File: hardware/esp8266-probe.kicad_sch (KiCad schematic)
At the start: 31 parts, among them J1 USB_C_Receptacle_USB2.0, J2 Debug, J3 Target, SW1 Reset, SW2 Flash, U1 LD1117DT33, U2 ESP-12E

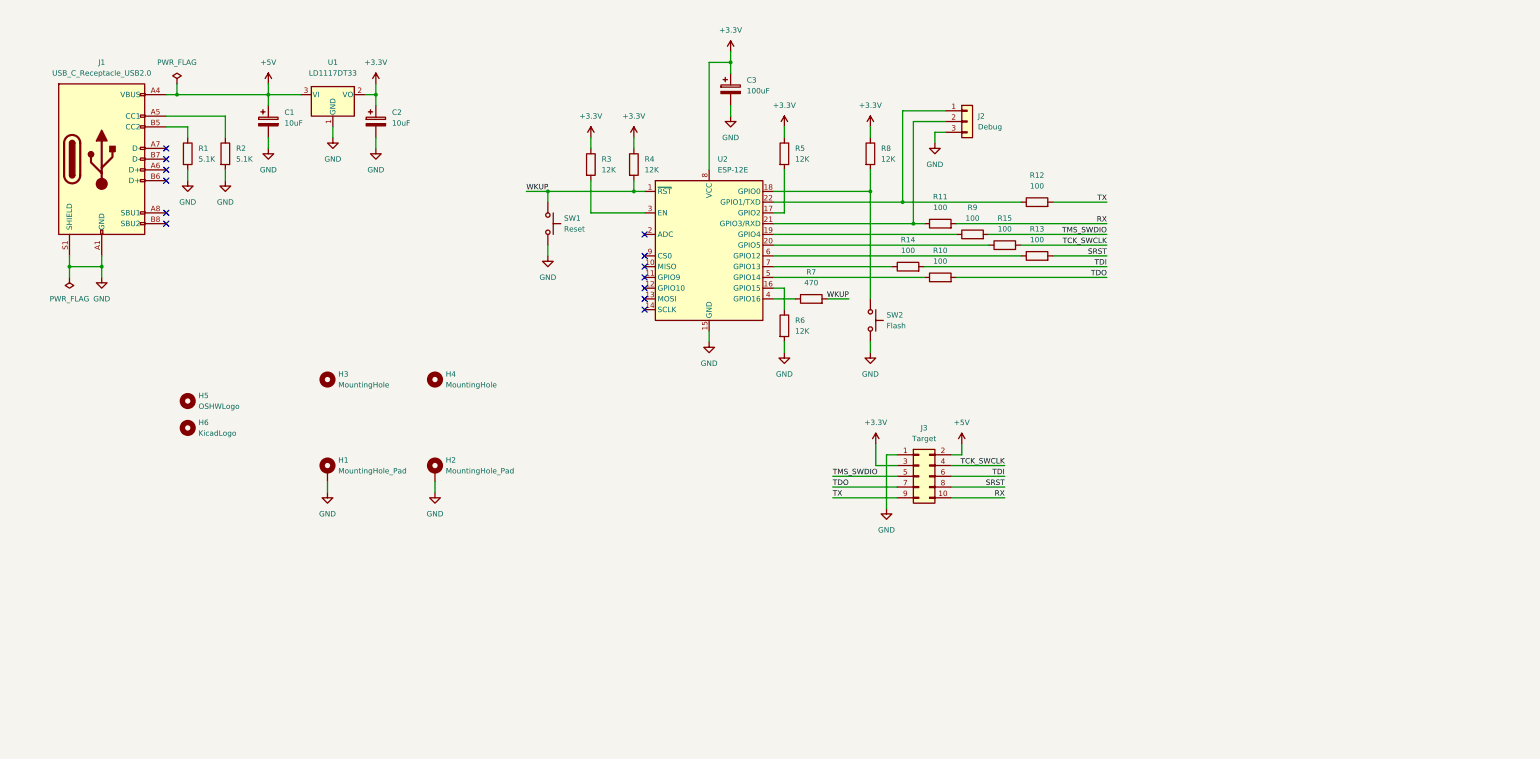
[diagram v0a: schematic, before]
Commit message: Added level shifters and power to the PCB.
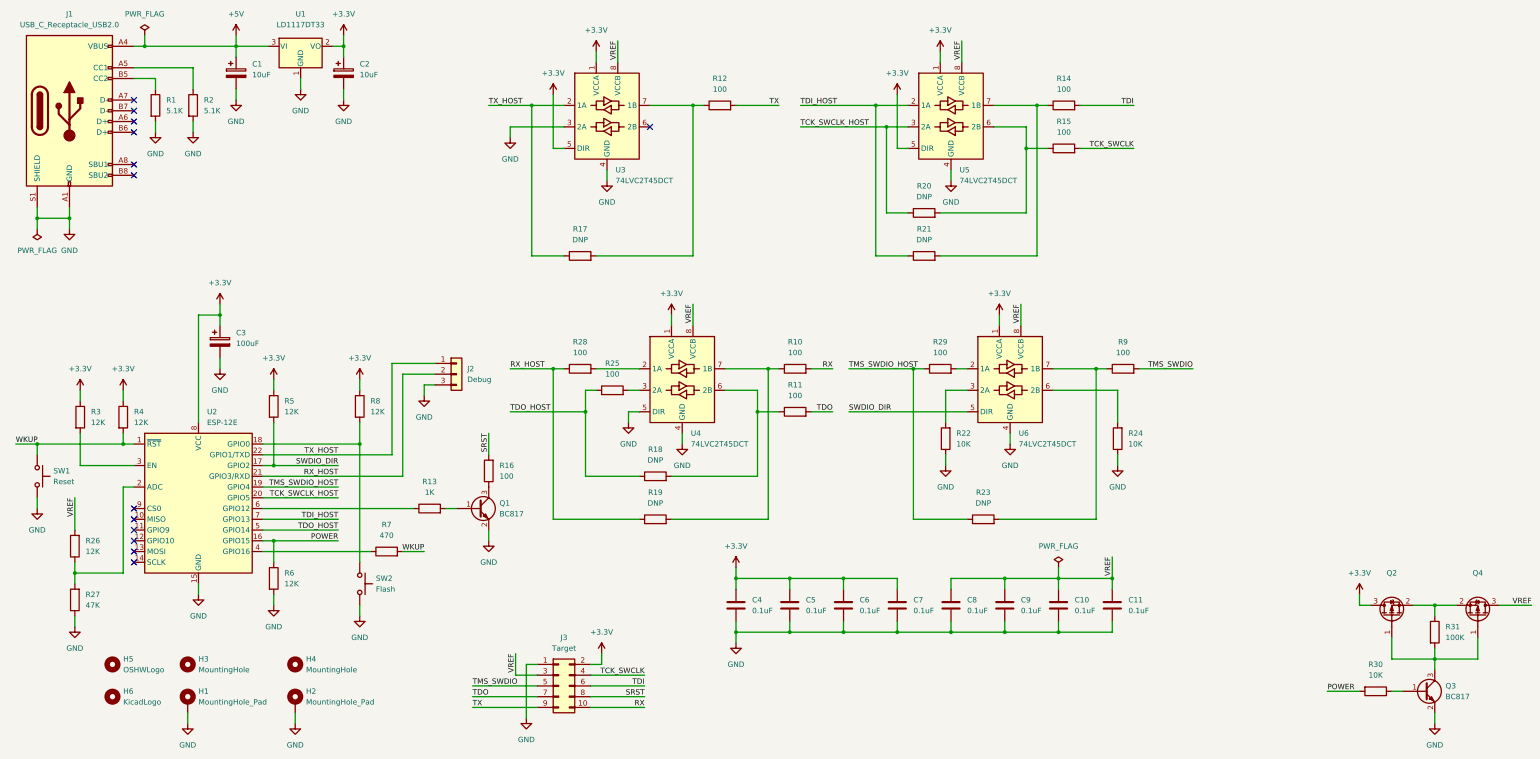
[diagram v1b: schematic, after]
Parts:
- added C10, C11, C4, C5, C6, C7, C8, C9: 0.1uF, Capacitor_SMD:C_0603_1608Metric, symbol Device:C
- added Q1, Q3: BC817, Package_TO_SOT_SMD:SOT-23, symbol Transistor_BJT:BC817
- added Q2: (no value), symbol Device:Q_PMOS_GSD
- added Q4: (no value), Package_TO_SOT_SMD:SOT-23, symbol Device:Q_PMOS_GSD
- added R16, R25, R28, R29: 100, Resistor_SMD:R_0603_1608Metric, symbol Device:R
- added R17, R18, R19, R20, R21, R23: DNP, Resistor_SMD:R_0603_1608Metric, symbol Device:R
- added R22, R24, R30: 10K, Resistor_SMD:R_0603_1608Metric, symbol Device:R
- added R26: 12K, Resistor_SMD:R_0603_1608Metric, symbol Device:R
- added R27: 47K, Resistor_SMD:R_0603_1608Metric, symbol Device:R
- added R31: 100K, Resistor_SMD:R_0603_1608Metric, symbol Device:R
- added U3, U4, U5, U6: 74LVC2T45DCT, Package_SO:VSSOP-8_3.0x3.0mm_P0.65mm, symbol Logic_LevelTranslator:74LVC2T45DC
- H5: footprint (none) -> Symbol:OSHW-Logo_5.7x6mm_SilkScreen
- H6: footprint (none) -> Symbol:KiCad-Logo2_5mm_SilkScreen
- R13: value 100 -> 1K
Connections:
- net +3V3: now also J3.2 (Pin_2), C4.1, C5.1, C6.1, C7.1, Q2.3 (D), U3.1 (VCCA), U3.5 (DIR), U4.1 (VCCA), U5.1 (VCCA), U5.5 (DIR), U6.1 (VCCA); no longer J3.3 (Pin_3)
- net +5V: no longer J3.2 (Pin_2)
- net GND: now also C10.2, C11.2, C4.2, C5.2, C6.2, C7.2, C8.2, C9.2, Q1.2 (E), Q3.2 (E), R22.1, R24.1, R27.1, U3.3 (2A), U3.4 (GND), U4.4 (GND), U4.5 (DIR), U5.4 (GND), U6.4 (GND)
- net RX: now also R10.2; no longer R11.2
- net SRST: now also R16.2; no longer R13.2
- net TDO: now also R11.2; no longer R10.2
- net at R9.1: now also R23.2, U6.7 (1B); no longer U2.19 (GPIO4)
- net POWER: now reaches R6.1, U2.16 (GPIO15)
- net POWER: now also R30.2
- net SWDIO_DIR: now reaches R5.2, U2.17 (GPIO2)
- net SWDIO_DIR: now also U6.5 (DIR)
- net at U2.2 (ADC): now also R26.1, R27.2
- net at R15.1: now also R20.2, U5.6 (2B); no longer U2.20 (GPIO5)
- net RX_HOST: now reaches J2.2 (Pin_2), U2.21 (GPIO3/RXD)
- net RX_HOST: now also R19.1, R28.1; no longer R11.1
- net TX_HOST: now reaches J2.1 (Pin_1), U2.22 (GPIO1/TXD)
- net TX_HOST: now also R17.1, U3.2 (1A); no longer R12.1
- net at R10.1: now also R19.2, U4.7 (1B); no longer U2.5 (GPIO14)
- net at R14.1: now also R21.2, U5.7 (1B); no longer U2.7 (GPIO13)
- new net: R28.2, U4.2 (1A)
- new net: R25.2, U4.3 (2A)
- new net: R11.1, R18.2, U4.6 (2B)
- new net: Q2.1 (G), Q3.3 (C), Q4.1 (G), R31.2
- new net: Q2.2 (S), Q4.2 (S), R31.1
- new net: R22.2, U6.3 (2A)
- new net: Q1.1 (B), R13.2
- new net: Q1.3 (C), R16.1
- new net: Q3.1 (B), R30.1
- new net: R29.2, U6.2 (1A)
- new net: R24.2, U6.6 (2B)
- new net: R12.1, R17.2, U3.7 (1B)
- new net TCK_SWCLK_HOST: R20.1, U2.20 (GPIO5), U5.3 (2A)
- new net TDI_HOST: R21.1, U2.7 (GPIO13), U5.2 (1A)
- new net TDO_HOST: R18.1, R25.1, U2.5 (GPIO14)
- new net TMS_SWDIO_HOST: R23.1, R29.1, U2.19 (GPIO4)
- new net VREF: C10.1, C11.1, C8.1, C9.1, J3.3 (Pin_3), Q4.3 (D), R26.2, U3.8 (VCCB), U4.8 (VCCB), U5.8 (VCCB), U6.8 (VCCB)
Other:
- moved on the sheet: C1, C2, C3, H1, H2, H3, H4, H5, H6, J1, J2, J3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
